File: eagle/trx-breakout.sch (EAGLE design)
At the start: 36 parts, among them J1 629722000214, J2 DF12NB(3.0)-10DP-0.5V, P1 S2B-PH-SM4-TB, Q1 BSS84

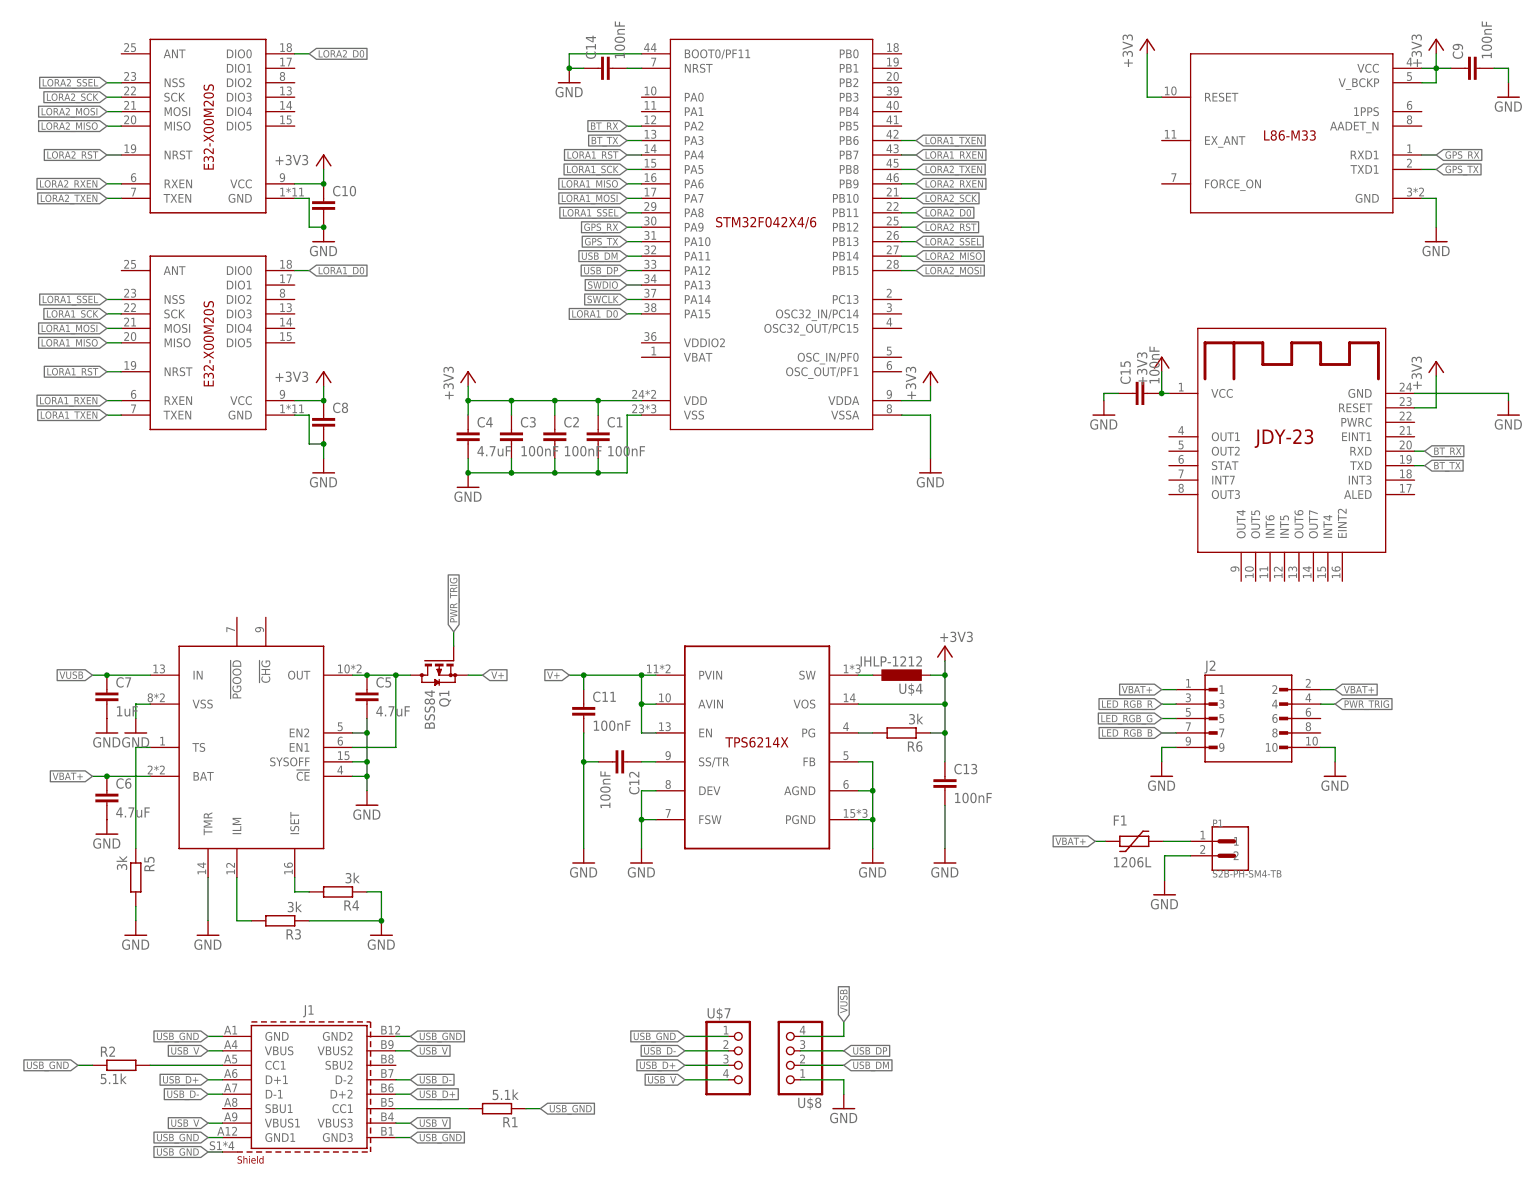
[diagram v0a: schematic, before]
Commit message: Added breakout board and progressed mainboard
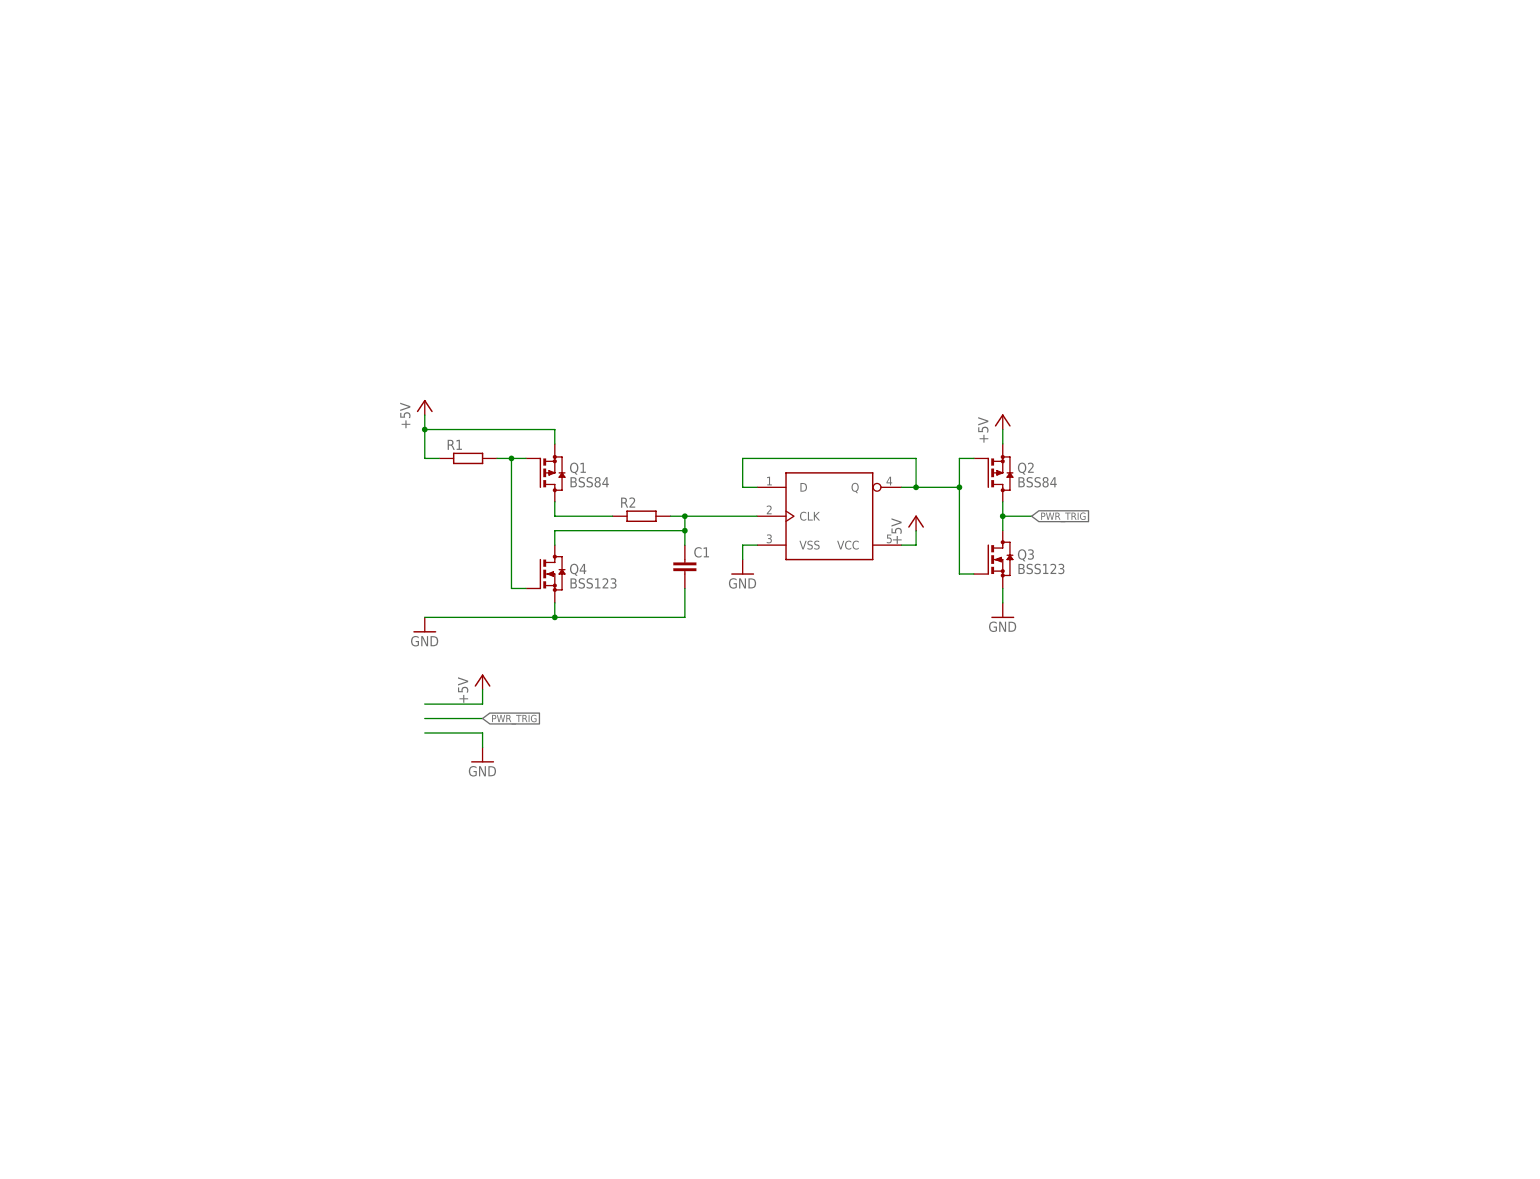
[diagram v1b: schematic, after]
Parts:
- removed C10, C4, C5, C6, C8: 4.7uF, rcl:C-EUC0805
- removed C11, C12, C13, C14, C15, C2, C3, C9: 100nF, rcl:C-EUC0805
- removed C7: 1uF, rcl:C-EUC0805
- removed F1: 1206L, ptc-littlefuse:1206L
- removed J1: 629722000214, Wurth_Connectors_WR-USB:629722000214
- removed J2: DF12NB(3.0)-10DP-0.5V, con-hirose2:DF12NB(3.0)-10DP-0.5V
- removed P1: S2B-PH-SM4-TB, con-jst2:S2B-PH-SM4-TB
- removed R3, R4, R5, R6: 3k, rcl:R-EU_R0805
- removed U$10: STM32-F042X4/6-48, st-microelectronics:STM32-F042X4/6-48
- removed U$2: TPS6214X, texas-instruments:TPS6214X
- removed U$3: BQ2407X, texas-instruments:BQ2407X
- removed U$4: IHLP-1212, inductor-vishay:IHLP-1212
- removed U$5: JDY-23, bluetooth:JDY-23
- removed U$6, U$9: E32-X00M20S, ebyte:E32-X00M20S
- removed U$7: BC034-04-A-V-0150-L-C, con-gct:BC034-04-A-V-0150-L-C
- removed U$8: BC075-04-A-L-A, con-gct:BC075-04-A-L-A
- added Q2: BSS84, transistor-small-signal:BSS84
- added Q3, Q4: BSS123, transistor-small-signal:BSS123
- C1: value 100nF -> (none)
- R1, R2: value 5.1k -> (none)
- U$1: value L86-M33 -> SN74LVC1G80; device quectel:L86-M33 -> texas-instruments:SN74LVC1G80
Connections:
- removed net +3V3: C1.1, C10.1, C13.1, C15.2, C2.1, C3.1, C4.1, C8.1, C9.1, R6.1, U$1.RESET, U$1.VCC, U$1.V_BCKP, U$10.VDD, U$10.VDDA, U$2.VOS, U$4.2, U$5.RESET, U$5.VCC, U$6.VCC, U$9.VCC
- removed net BT_RX: U$10.PA2, U$5.RXD
- removed net BT_TX: U$10.PA3, U$5.TXD
- removed net GPS_RX: U$1.RXD1, U$10.PA9
- removed net GPS_TX: U$1.TXD1, U$10.PA10
- removed net LED_RGB_B: J2.7
- removed net LED_RGB_G: J2.5
- removed net LED_RGB_R: J2.3
- removed net LORA1_D0: U$10.PA15, U$9.DIO0
- removed net LORA1_MISO: U$10.PA6, U$9.MISO
- removed net LORA1_MOSI: U$10.PA7, U$9.MOSI
- removed net LORA1_RST: U$10.PA4, U$9.NRST
- removed net LORA1_RXEN: U$10.PB7, U$9.RXEN
- removed net LORA1_SCK: U$10.PA5, U$9.SCK
- removed net LORA1_SSEL: U$10.PA8, U$9.NSS
- removed net LORA1_TXEN: U$10.PB6, U$9.TXEN
- removed net LORA2_D0: U$10.PB11, U$6.DIO0
- removed net LORA2_MISO: U$10.PB14, U$6.MISO
- removed net LORA2_MOSI: U$10.PB15, U$6.MOSI
- removed net LORA2_RST: U$10.PB12, U$6.NRST
- removed net LORA2_RXEN: U$10.PB9, U$6.RXEN
- removed net LORA2_SCK: U$10.PB10, U$6.SCK
- removed net LORA2_SSEL: U$10.PB13, U$6.NSS
- removed net LORA2_TXEN: U$10.PB8, U$6.TXEN
- removed net N$10: U$2.AGND, U$2.FB, U$2.PGND
- removed net N$11: C14.2, U$10.NRST
- removed net N$12: F1.2, P1.1
- removed net N$4: R4.2, U$3.ISET
- removed net N$6: U$2.SW, U$4.1
- removed net N$7: C12.1, U$2.SS/TR
- removed net N$8: R6.2, U$2.PG
- removed net N$9: C5.1, Q1.D, U$3.EN1, U$3.OUT
- removed net SWCLK: U$10.PA14
- removed net SWDIO: U$10.PA13
- removed net USB_D+: J1.D+1, J1.D+2, U$7.3
- removed net USB_D-: J1.D-1, J1.D-2, U$7.2
- removed net USB_DM: U$10.PA11, U$8.2
- removed net USB_DP: U$10.PA12, U$8.3
- removed net USB_GND: J1.GND, J1.GND1, J1.GND2, J1.GND3, J1.SHIELD, R1.1, R2.1, U$7.1
- removed net USB_V: J1.VBUS, J1.VBUS1, J1.VBUS2, J1.VBUS3, U$7.4
- removed net V+: C11.1, Q1.S, U$2.AVIN, U$2.EN, U$2.PVIN
- removed net VBAT+: C6.1, F1.1, J2.1, J2.2, U$3.BAT
- removed net VUSB: C7.1, U$3.IN, U$8.4
- new net +5V: Q1.S, Q2.S, R1.1, U$1.VCC
- net GND: now also Q3.S, Q4.S, U$1.VSS; no longer C10.2, C11.2, C12.2, C13.2, C14.1, C15.1, C2.2, C3.2, C4.2, C5.2, C6.2, C7.2, C8.2, C9.2, J2.10, J2.9, P1.2, R3.1, R4.1, R5.2, U$1.GND, U$10.BOOT0/PF11, U$10.VSS, U$10.VSSA, U$2.DEV, U$2.FSW, U$3.!CE, U$3.EN2, U$3.SYSOFF, U$3.TMR, U$3.VSS, U$5.GND, U$6.GND, U$8.1, U$9.GND
- net N$1: now also Q1.G, Q4.G, R1.2; no longer J1.CC1@1, R2.2
- net N$2: now also Q1.D, R2.1; no longer J1.CC1@2, R1.2
- net N$3: now also C1.1, Q4.D, R2.2, U$1.CLK; no longer R3.2, U$3.ILM
- net N$5: now also Q2.G, Q3.G, U$1.D, U$1.Q; no longer R5.1, U$3.TS
- net PWR_TRIG: now also Q2.D, Q3.D; no longer J2.4, Q1.G
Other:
- moved on the sheet: C1, Q1, R1, R2

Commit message: Added basic auto-route
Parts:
- added J1: DF12NB(3.0)-10DX-0.5VHRS_DF12NB(3.0)-10DS-0.5V, con-hirose2:DF12NB(3.0)-10DX-0.5VHRS_DF12NB(3.0)-10DS-0.5V
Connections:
- new net N$10: J1.8
- new net N$8: J1.4
- new net N$9: J1.6
- net +5V: now also J1.1, J1.2
- net GND: now also J1.10, J1.9
- net PWR_TRIG: now also J1.3
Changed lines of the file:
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@@
 <part name="P+3" library="supply1" library_urn="urn:adsk.eagle:library:371" deviceset="+5V" device=""/>
 <part name="GND3" library="supply1" library_urn="urn:adsk.eagle:library:371" deviceset="GND" device=""/>
-<part name="GND4" library="supply1" library_urn="urn:adsk.eagle:library:371" deviceset="GND" device=""/>
 <part name="P+4" library="supply1" library_urn="urn:adsk.eagle:library:371" deviceset="+5V" device=""/>
+<part name="J1" library="con-hirose2" library_urn="urn:adsk.eagle:library:40899389" deviceset="DF12NB(3.0)-10DX-0.5V" device="HRS_DF12NB(3.0)-10DS-0.5V" package3d_urn="urn:adsk.eagle:package:40903384/2"/>
+<part name="GND5" library="supply1" library_urn="urn:adsk.eagle:library:371" deviceset="GND" device=""/>
+<part name="GND6" library="supply1" library_urn="urn:adsk.eagle:library:371" deviceset="GND" device=""/>
+<part name="P+5" library="supply1" library_urn="urn:adsk.eagle:library:371" deviceset="+5V" device=""/>
 </parts>
 <sheets>
@@
 <attribute name="VALUE" x="177.8" y="99.06" size="1.778" layer="96"/>
 </instance>
-<instance part="GND4" gate="1" x="88.9" y="76.2" smashed="yes">
-<attribute name="VALUE" x="86.36" y="73.66" size="1.778" layer="96"/>
-</instance>
-<instance part="P+4" gate="1" x="88.9" y="91.44" smashed="yes">
-<attribute name="VALUE" x="86.36" y="86.36" size="1.778" layer="96" rot="R90"/>
+<instance part="P+4" gate="1" x="142.24" y="93.98" smashed="yes">
+<attribute name="VALUE" x="139.7" y="88.9" size="1.778" layer="96" rot="R90"/>
+</instance>
+<instance part="J1" gate="G$1" x="127" y="83.82" smashed="yes">
+<attribute name="NAME" x="119.38" y="92.202" size="1.778" layer="95"/>
+</instance>
+<instance part="GND5" gate="1" x="111.76" y="73.66" smashed="yes">
+<attribute name="VALUE" x="109.22" y="71.12" size="1.778" layer="96"/>
+</instance>
+<instance part="GND6" gate="1" x="142.24" y="73.66" smashed="yes">
+<attribute name="VALUE" x="139.7" y="71.12" size="1.778" layer="96"/>
+</instance>
+<instance part="P+5" gate="1" x="111.76" y="93.98" smashed="yes">
+<attribute name="VALUE" x="109.22" y="88.9" size="1.778" layer="96" rot="R90"/>
 </instance>
 </instances>
@@
 <segment>
 <pinref part="P+4" gate="1" pin="+5V"/>
-<wire x1="78.74" y1="86.36" x2="88.9" y2="86.36" width="0.1524" layer="91"/>
-<wire x1="88.9" y1="86.36" x2="88.9" y2="88.9" width="0.1524" layer="91"/>
+<wire x1="139.7" y1="88.9" x2="142.24" y2="88.9" width="0.1524" layer="91"/>
+<wire x1="142.24" y1="88.9" x2="142.24" y2="91.44" width="0.1524" layer="91"/>
+<pinref part="J1" gate="G$1" pin="2"/>
+</segment>
+<segment>
+<pinref part="J1" gate="G$1" pin="1"/>
+<wire x1="114.3" y1="88.9" x2="111.76" y2="88.9" width="0.1524" layer="91"/>
+<wire x1="111.76" y1="88.9" x2="111.76" y2="91.44" width="0.1524" layer="91"/>
+<pinref part="P+5" gate="1" pin="+5V"/>
 </segment>
 </net>
@@
 </segment>
 <segment>
-<pinref part="GND4" gate="1" pin="GND"/>
-<wire x1="78.74" y1="81.28" x2="88.9" y2="81.28" width="0.1524" layer="91"/>
-<wire x1="88.9" y1="81.28" x2="88.9" y2="78.74" width="0.1524" layer="91"/>
+<pinref part="J1" gate="G$1" pin="9"/>
+<wire x1="114.3" y1="78.74" x2="111.76" y2="78.74" width="0.1524" layer="91"/>
+<wire x1="111.76" y1="78.74" x2="111.76" y2="76.2" width="0.1524" layer="91"/>
+<pinref part="GND5" gate="1" pin="GND"/>
+</segment>
+<segment>
+<pinref part="J1" gate="G$1" pin="10"/>
+<wire x1="139.7" y1="78.74" x2="142.24" y2="78.74" width="0.1524" layer="91"/>
+<wire x1="142.24" y1="78.74" x2="142.24" y2="76.2" width="0.1524" layer="91"/>
+<pinref part="GND6" gate="1" pin="GND"/>
 </segment>
 </net>
@@
 </segment>
 <segment>
-<wire x1="78.74" y1="83.82" x2="88.9" y2="83.82" width="0.1524" layer="91"/>
-<label x="88.9" y="83.82" size="1.27" layer="95" xref="yes"/>
-</segment>
-</net>
+<label x="111.76" y="86.36" size="1.27" layer="95" rot="R180" xref="yes"/>
+<pinref part="J1" gate="G$1" pin="3"/>
+<wire x1="114.3" y1="86.36" x2="111.76" y2="86.36" width="0.1524" layer="91"/>
+</segment>
+</net>
+<net name="N$8" class="0">
+<segment>
+<pinref part="J1" gate="G$1" pin="4"/>
+<wire x1="139.7" y1="86.36" x2="142.24" y2="86.36" width="0.1524" layer="91"/>
+</segment>
+</net>
+<net name="N$9" class="0">
+<segment>
+<pinref part="J1" gate="G$1" pin="6"/>
+<wire x1="139.7" y1="83.82" x2="142.24" y2="83.82" width="0.1524" layer="91"/>
+</segment>
+</net>
+<net name="N$10" class="0">
+<segment>
+<pinref part="J1" gate="G$1" pin="8"/>
+<wire x1="139.7" y1="81.28" x2="142.24" y2="81.28" width="0.1524" layer="91"/>
+</segment>
+</net>

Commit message: Finalized alpha design
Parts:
- added C2: 2.2uF, rcl:C-EUC0805
- added C3: 4.7uF, rcl:C-EUC0805
- added U$2: PTS530, switches-ck:PTS530
- added U$3: TPS61240, texas-instruments:TPS61240
- added U$4: 1uH, inductor-vishay:IHLP-1212
- added U$5, U$6, U$7: ARGB_LED, led:ARGB_LED
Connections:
- removed net N$10: J1.8
- removed net N$8: J1.4
- removed net N$9: J1.6
- new net +3V3: C2.1, J1.2, U$3.EN, U$3.VIN, U$4.1
- new net LED_D: J1.4, U$5.DIN, U$6.DIN, U$7.DIN
- new net N$6: Q1.G, Q4.G, R1.2, U$2.S, U$2.S@1
- new net VBAT: J1.1, Q1.S, R1.1
- net +5V: now also C3.1, U$3.FB, U$3.VOUT, U$5.VDD, U$6.VDD, U$7.VDD; no longer J1.1, J1.2, Q1.S, R1.1
- net GND: now also C2.2, C3.2, U$2.P, U$2.P@1, U$3.GND, U$5.VSS, U$6.VSS
- net N$1: now also U$3.L, U$4.2; no longer Q1.G, Q4.G, R1.2
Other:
- moved on the sheet: C1, J1, Q1, Q2, Q3, Q4, R1, R2

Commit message: Added new layout and gerber files
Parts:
- C1: value (none) -> 2.2uF
- C2: value 2.2uF -> 4.7uF
- R1: value (none) -> 100k
- R2: value (none) -> 200k
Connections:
- new net N$4: Q1.G, Q3.G, R1.2, U$2.S, U$2.S@1
- new net N$7: Q2.S
- net +3V3: now also C1.1; no longer C2.1
- net +5V: now also C2.1; no longer C3.1, Q2.S, U$1.VCC
- net GND: now also U$7.VSS
- net N$3: now also C3.1, Q3.D; no longer C1.1, Q4.D
- net N$5: now also Q4.G; no longer Q3.G
- net N$6: now also U$1.VCC; no longer Q1.G, Q4.G, R1.2, U$2.S, U$2.S@1
- net PWR_TRIG: now also Q4.D; no longer Q3.D
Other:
- moved on the sheet: C1, C2, C3, Q3, Q4
